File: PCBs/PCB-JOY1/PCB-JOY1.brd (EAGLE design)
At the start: 29 x 29 mm, 6 parts

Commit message: asdf
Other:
- board text added: "GITHUB: SKAARHOJ-Open-Engineering"
- board text added: "PCB-JOY1"
- board text added: "SKAARHOJ 2013"
- board text added: "v22-04-13"
- board text removed: "Fusion: 60199"
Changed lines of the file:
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@@
 <?xml version="1.0" encoding="utf-8"?>
 <!DOCTYPE eagle SYSTEM "eagle.dtd">
-<eagle version="6.2">
+<eagle version="6.4">
 <drawing>
 <settings>
@@
 <hole x="26.5" y="2.5" drill="3.2"/>
 <hole x="2.5" y="2.5" drill="3.2"/>
-<text x="14.605" y="0.635" size="0.8128" layer="121">Fusion: 60199</text>
+<wire x1="17.145" y1="19.05" x2="17.145" y2="15.875" width="0.4064" layer="122"/>
+<wire x1="17.145" y1="15.875" x2="20.32" y2="15.875" width="0.4064" layer="122"/>
+<wire x1="20.32" y1="15.875" x2="20.32" y2="19.05" width="0.4064" layer="122"/>
+<wire x1="20.32" y1="19.05" x2="17.145" y2="19.05" width="0.4064" layer="122"/>
+<wire x1="17.145" y1="10.16" x2="17.145" y2="6.985" width="0.4064" layer="122"/>
+<wire x1="17.145" y1="6.985" x2="19.05" y2="6.985" width="0.4064" layer="122"/>
+<wire x1="19.05" y1="6.985" x2="20.32" y2="8.255" width="0.4064" layer="122"/>
+<wire x1="20.32" y1="8.255" x2="20.32" y2="10.16" width="0.4064" layer="122"/>
+<wire x1="20.32" y1="10.16" x2="17.145" y2="10.16" width="0.4064" layer="122"/>
+<text x="23.114" y="0.4572" size="1.016" layer="122" rot="MR0">PCB-JOY1</text>
+<text x="28.3718" y="23.7998" size="1.524" layer="122" rot="MR270">SKAARHOJ 2013</text>
+<text x="5.842" y="1.27" size="0.8128" layer="122" rot="MR180">v22-04-13</text>
+<text x="5.334" y="26.3525" size="0.8128" layer="122" font="vector" rot="MR270">GITHUB: SKAARHOJ-Open-Engineering</text>
 </plain>
 <attributes>
@@
 </class>
 </classes>
-<designrules>
+<designrules name="default">
 <description language="de">&lt;b&gt;EAGLE Design Rules&lt;/b&gt;
 &lt;p&gt;
@@
 </autorouter>
 <elements>
-<element name="U$1" library="SKAARHOJ" package="PLAYSTATION2_ANALOG_JOYSTICK" value="PLAYSTATION2_ANALOG_JOYSTICK" x="14.5" y="14.5" rot="R90"/>
-<element name="JOY1" library="SparkFun" package="2X4" value="M04X2" x="14.605" y="19.05" rot="MR0"/>
-<element name="JOY2" library="SparkFun" package="2X4" value="M04X2" x="14.605" y="10.16" rot="MR0"/>
+<element name="U$1" library="SKAARHOJ" package="PLAYSTATION2_ANALOG_JOYSTICK" value="PLAYSTATION2_ANALOG_JOYSTICK" x="14.5" y="14.5" smashed="yes" rot="R90"/>
+<element name="JOY1" library="SparkFun" package="2X4" value="M04X2" x="14.605" y="19.05" smashed="yes" rot="MR0">
+<attribute name="NAME" x="19.685" y="22.225" size="1.27" layer="26" ratio="10" rot="MR0"/>
+</element>
+<element name="JOY2" library="SparkFun" package="2X4" value="M04X2" x="14.605" y="10.16" smashed="yes" rot="MR0">
+<attribute name="NAME" x="19.685" y="13.335" size="1.27" layer="26" ratio="10" rot="MR0"/>
+</element>
 <element name="C1" library="SparkFun" package="0603-CAP" value="10nF" x="7.62" y="26.67" rot="MR90"/>
 <element name="C2" library="SparkFun" package="0603-CAP" value="10nF" x="10.16" y="26.67" rot="MR90"/>

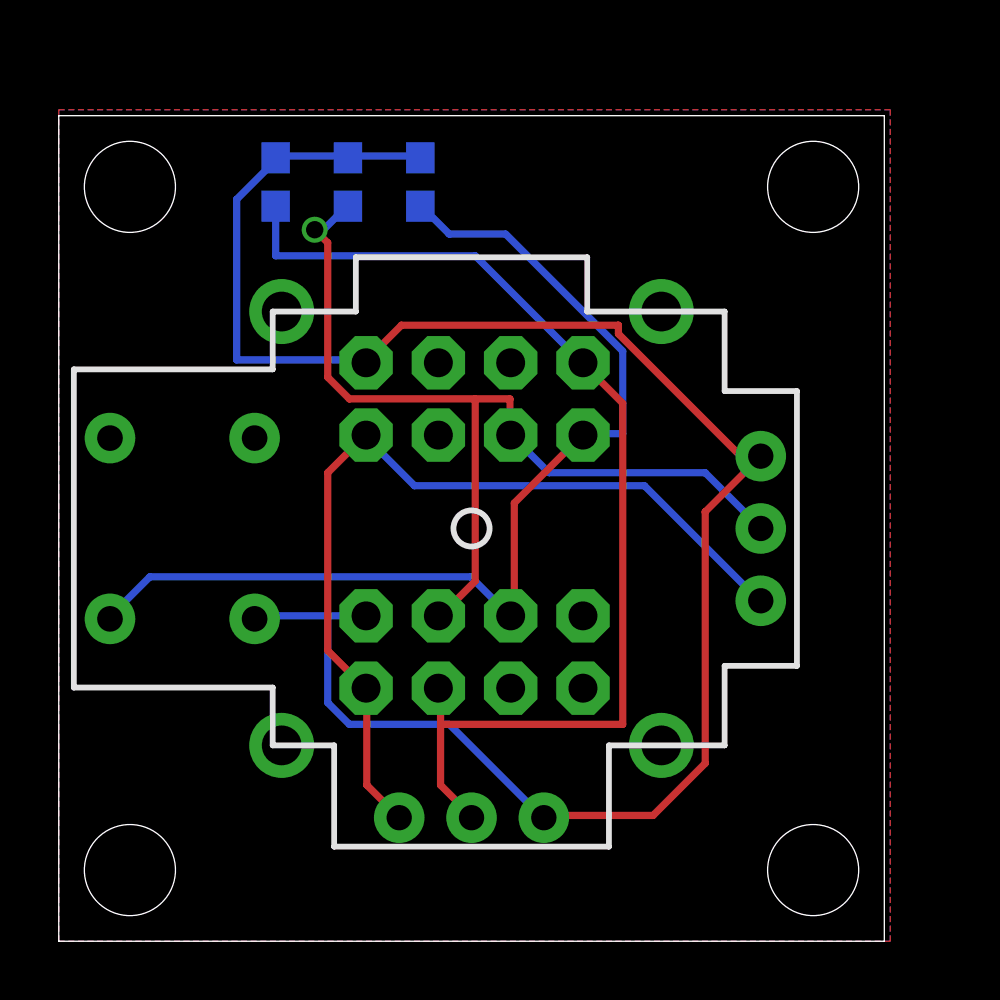
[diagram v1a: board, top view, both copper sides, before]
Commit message: Large revisions of boards, change of forms, in particular all mounting holes now has a 7mm diameter and fully inside the board.
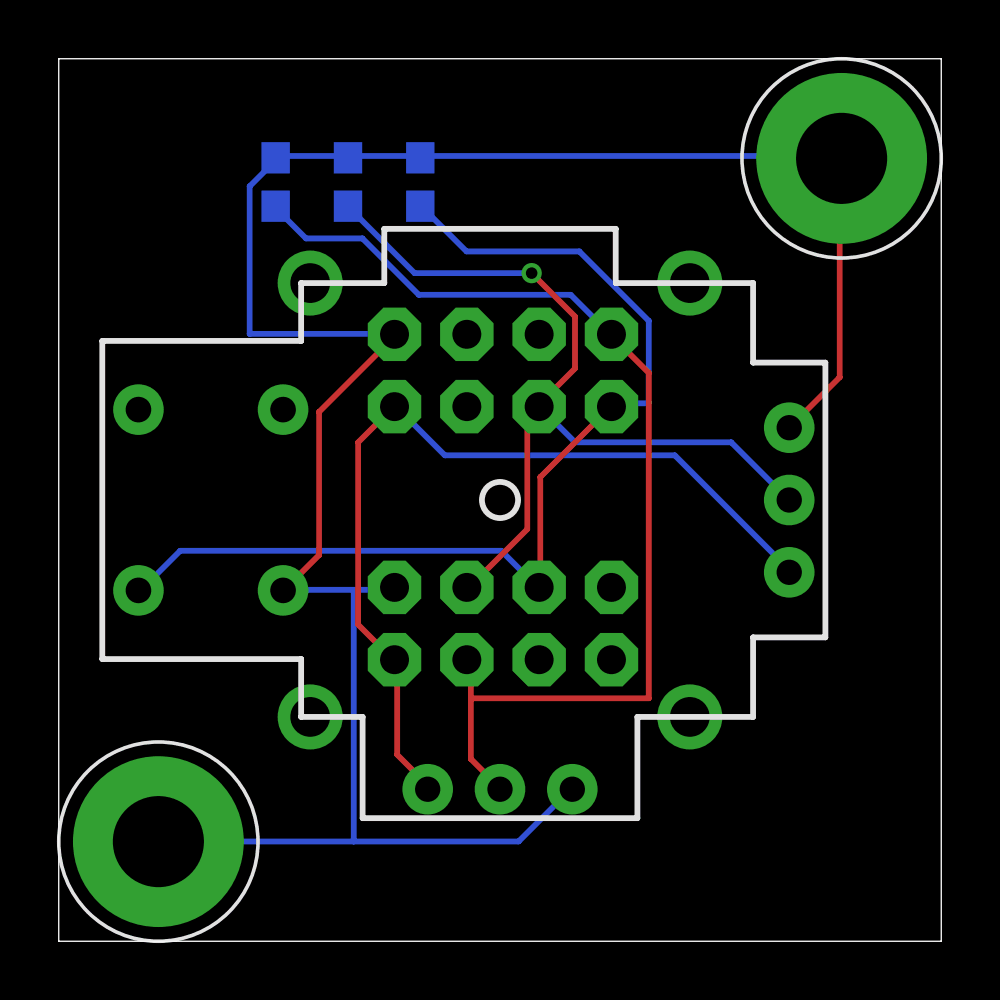
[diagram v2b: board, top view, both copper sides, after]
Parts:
- removed U$1: PLAYSTATION2_ANALOG_JOYSTICK, SKAARHOJ:PLAYSTATION2_ANALOG_JOYSTICK
- added JOYSTICK: PLAYSTATION2_ANALOG_JOYSTICK, SKAARHOJ:PLAYSTATION2_ANALOG_JOYSTICK
- added U$15, U$20: GNDPAD6MM, SKAARHOJ:3.2MMPAD6MM
- moved JOY1 1.41 mm to (15.6, 20.1)
- moved JOY2 1.41 mm to (15.6, 11.2)
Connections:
- net 5V: now also JOYSTICK.H1, JOYSTICK.V1; no longer U$1.H1, U$1.V1
- net GND: now also JOYSTICK.B2A, JOYSTICK.H3, JOYSTICK.V3, U$15.P$1, U$20.P$1; no longer U$1.B2A, U$1.H3, U$1.V3
- net POT1: now also JOYSTICK.V2; no longer U$1.V2
- net POT2: now also JOYSTICK.H2; no longer U$1.H2
- net SW: now also JOYSTICK.B1A; no longer U$1.B1A
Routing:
- net GND: track 68.5 -> 80.7 mm
- net POT2: track 33.2 -> 30.9 mm
- net POT1: track 38.8 -> 38.3 mm
- removed copper zone on layer 1, net GND
- removed copper zone on layer 16, net GND
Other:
- board size 29 x 29 mm -> 31 x 31 mm

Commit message: Updated boards
Updated boards with logo before first sending to Alma.
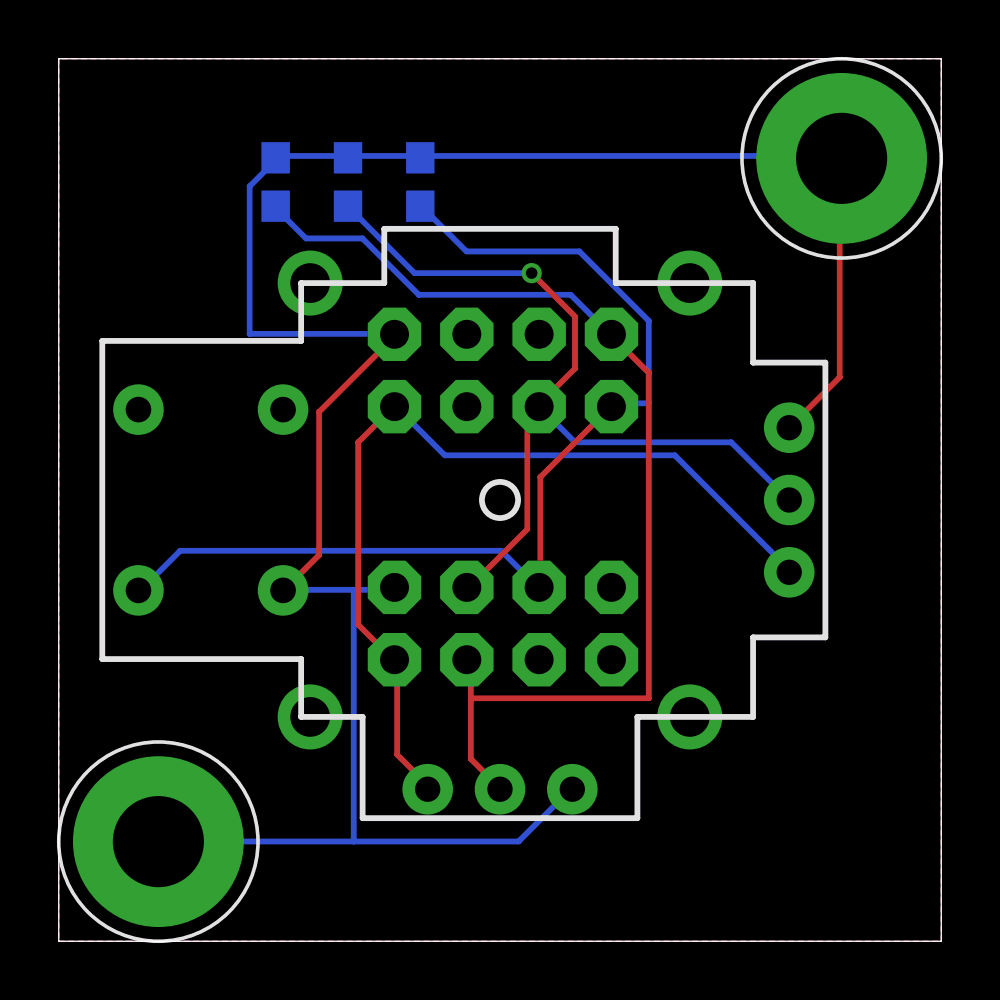
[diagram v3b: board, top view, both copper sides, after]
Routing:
- added copper zone on layer 1, net GND
- added copper zone on layer 16, net GND
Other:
- board text added: "v07-13"
- board text removed: "v22-04-13"

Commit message: PCB updates
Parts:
- removed JOY1, JOY2: M04X2, SparkFun:2X4
- added C11, C15, C16: 100nF, SparkFun:0603-CAP
- added C17: 10uF, SparkFun:0805
- added C9: 22uF, SparkFun:0805
- added IC5: ADS7828, burr-brown:TSSOP16-PW
- added L4: ILHB0805ER121V, SparkFun:0805
- added R3: 0R, SparkFun:0603-RES
- added R4: 10k, SparkFun:0603-RES
- added SERIAL1: M04X2M2X4SMALLER, SKAARHOJ:M2X4SMALLER
- added U$19: 2BITADDRSMALL, SKAARHOJ:2BITADDR_SMALL
- moved C1 20.7 mm to (16.7, 8.02), turned to 180 degrees
- moved C2 16.8 mm to (22.3, 15.2), turned to 0 degrees
- moved C3 14.4 mm to (4.70, 14.7)
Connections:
- removed net POT1: C1.1, JOY1.2, JOY2.5, JOYSTICK.V2
- removed net POT2: C2.1, JOY1.3, JOY2.6, JOYSTICK.H2
- removed net SW: C3.1, JOY1.1, JOY2.4, JOYSTICK.B1A
- new net 5V_AD: C15.1, C16.1, C17.1, IC5.10, IC5.16, R3.2
- new net A1: IC5.12, U$19.A0, U$19.AS0
- new net A2: IC5.13, U$19.A1, U$19.AS1
- new net FRONT: C3.1, IC5.1, JOYSTICK.B1A, R4.2
- new net I2C_SCL: IC5.14, SERIAL1.4
- new net I2C_SDA: IC5.15, SERIAL1.3
- new net JOY_1: C1.1, IC5.3, JOYSTICK.V2
- new net JOY_2: C2.1, IC5.4, JOYSTICK.H2
- new net N$1: C11.1, L4.1, SERIAL1.2
- net 5V: now also C9.1, L4.2, R3.1, R4.1, U$19.H0, U$19.H1; no longer JOY1.7, JOY2.7
- net GND: now also C11.2, C15.2, C16.2, C17.2, C9.2, IC5.11, IC5.9, SERIAL1.1, U$19.L0, U$19.L1; no longer JOY1.8, JOY2.8
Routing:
- net FRONT: track 0.00 -> 52.9 mm
- net A1: track 0.00 -> 40.3 mm
- net POT1: track 38.3 -> 0.00 mm
- net SW: track 36.5 -> 0.00 mm
- net GND: track 80.7 -> 116.6 mm
- net 5V: track 31.3 -> 63.7 mm, vias 0 -> 1
- net POT2: track 30.9 -> 0.00 mm, vias 1 -> 0
- net I2C_SDA: track 0.00 -> 25.5 mm, vias 0 -> 1
- net A2: track 0.00 -> 20.1 mm, vias 0 -> 1
- net 5V_AD: track 0.00 -> 16.8 mm, vias 0 -> 2
- net I2C_SCL: track 0.00 -> 14.9 mm
- net JOY_1: track 0.00 -> 9.98 mm
- net JOY_2: track 0.00 -> 8.55 mm
- net N$1: track 0.00 -> 6.53 mm
- removed copper zone on layer 1, net GND
- removed copper zone on layer 16, net GND
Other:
- board text added: "PCB-JOY1, v02-16"
- board text removed: "GITHUB: SKAARHOJ-Open-Engineering"
- board text removed: "PCB-JOY1"
- board text removed: "SKAARHOJ 2013"
- board text removed: "v07-13"

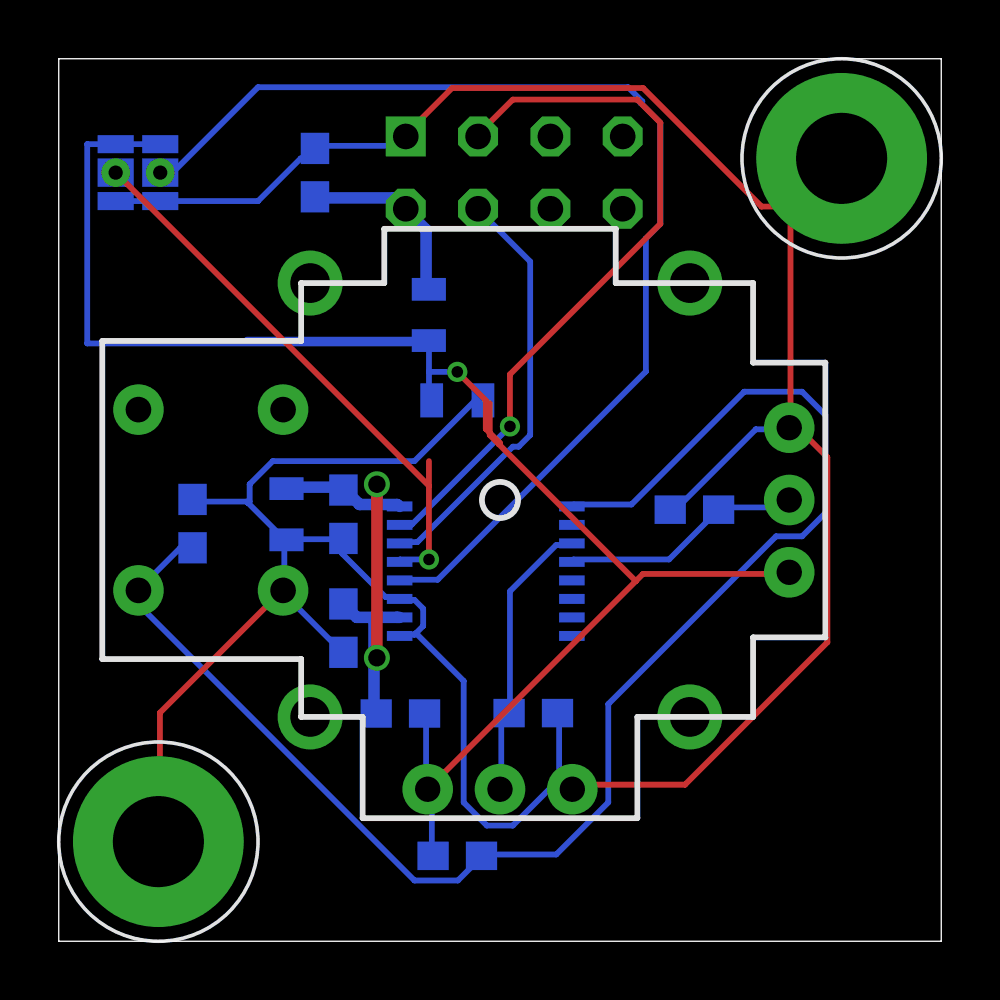
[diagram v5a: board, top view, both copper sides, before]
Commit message: Modified circuitry around AD converter on a number of PCBs
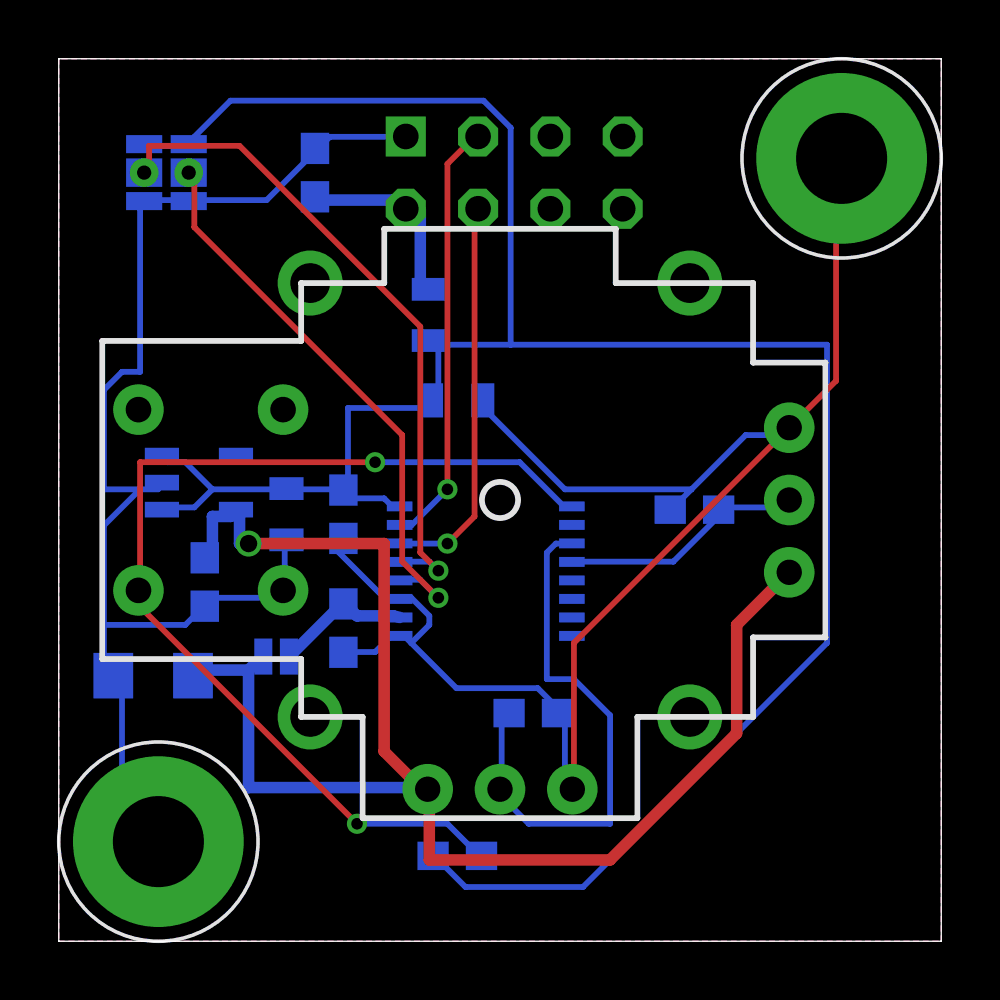
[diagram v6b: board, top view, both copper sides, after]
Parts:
- removed C3: 10nF, SparkFun:0603-CAP
- removed R3: 0R, SparkFun:0603-RES
- added C5: 100nF, SparkFun:0603-CAP
- added C8: 10uF 6.3V A TANT, freetronics:EIA3216
- added SJ1: SOLDERJUMPERNO, SparkFun:SJ_2S-NO
- added U2: MIC5205-3.3YM5, microbuilder:SOT23-5
- moved U$19 1.00 mm to (3.00, 27.0)
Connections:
- new net REF: C5.1, C8.A, JOYSTICK.H1, JOYSTICK.V1, SJ1.1, U2.5
- net 5V: now also C16.1, C17.1, IC5.16, U2.1, U2.3; no longer JOYSTICK.H1, JOYSTICK.V1, R3.1
- net 5V_AD: now also SJ1.2; no longer C16.1, C17.1, IC5.16, R3.2
- net FRONT: no longer C3.1
- net GND: now also C5.2, C8.C, U2.2; no longer C3.2
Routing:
- net REF: track 0.00 -> 53.0 mm, vias 0 -> 1
- net 5V: track 63.7 -> 83.9 mm, vias 1 -> 0
- net A1: track 40.3 -> 20.5 mm, vias 0 -> 1
- net FRONT: track 52.9 -> 36.5 mm, vias 0 -> 2
- net 5V_AD: track 16.8 -> 4.81 mm, vias 2 -> 0
- net I2C_SDA: track 25.5 -> 15.1 mm
- net GND: track 116.6 -> 106.9 mm
- net JOY_1: track 9.98 -> 19.4 mm
- net A2: track 20.1 -> 23.6 mm
- net I2C_SCL: track 14.9 -> 13.9 mm, vias 0 -> 1
- added copper zone on layer 1, net GND
- added copper zone on layer 16, net GND
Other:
- board text added: "PCB-JOY1, v11-16"
- board text removed: "PCB-JOY1, v02-16"

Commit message: d
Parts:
- added C3: 1nF, SparkFun:0603-CAP
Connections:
- new net N$2: C3.1, U2.4
- net GND: now also C3.2
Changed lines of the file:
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@@
 <element name="C5" library="SparkFun" package="0603-CAP" value="100nF" x="5.13" y="12.62" rot="MR270"/>
 <element name="C8" library="freetronics" package="EIA3216" value="10uF 6.3V A TANT" x="3.315" y="9.33" rot="MR180"/>
+<element name="C3" library="SparkFun" package="0603-CAP" value="1nF" x="-23" y="-28"/>
 </elements>
 <signals>
@@
 <vertex x="0" y="31"/>
 </polygon>
+<contactref element="C3" pad="2"/>
+<wire x1="2.2225" y1="3.81" x2="-22.15" y2="-28" width="0" layer="19" extent="1-16"/>
 </signal>
 <signal name="I2C_SDA">
@@
 <via x="6.6675" y="13.97" extent="1-16" drill="0.6096"/>
 </signal>
+<signal name="N$2">
+<contactref element="U2" pad="4"/>
+<contactref element="C3" pad="1"/>
+<wire x1="6.2251" y1="17.06" x2="-23.85" y2="-28" width="0" layer="19" extent="1-16"/>
+</signal>
 </signals>
